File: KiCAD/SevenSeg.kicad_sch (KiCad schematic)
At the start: 34 parts, among them J201 Input, J202 Output, U201 AZ1117-5.0

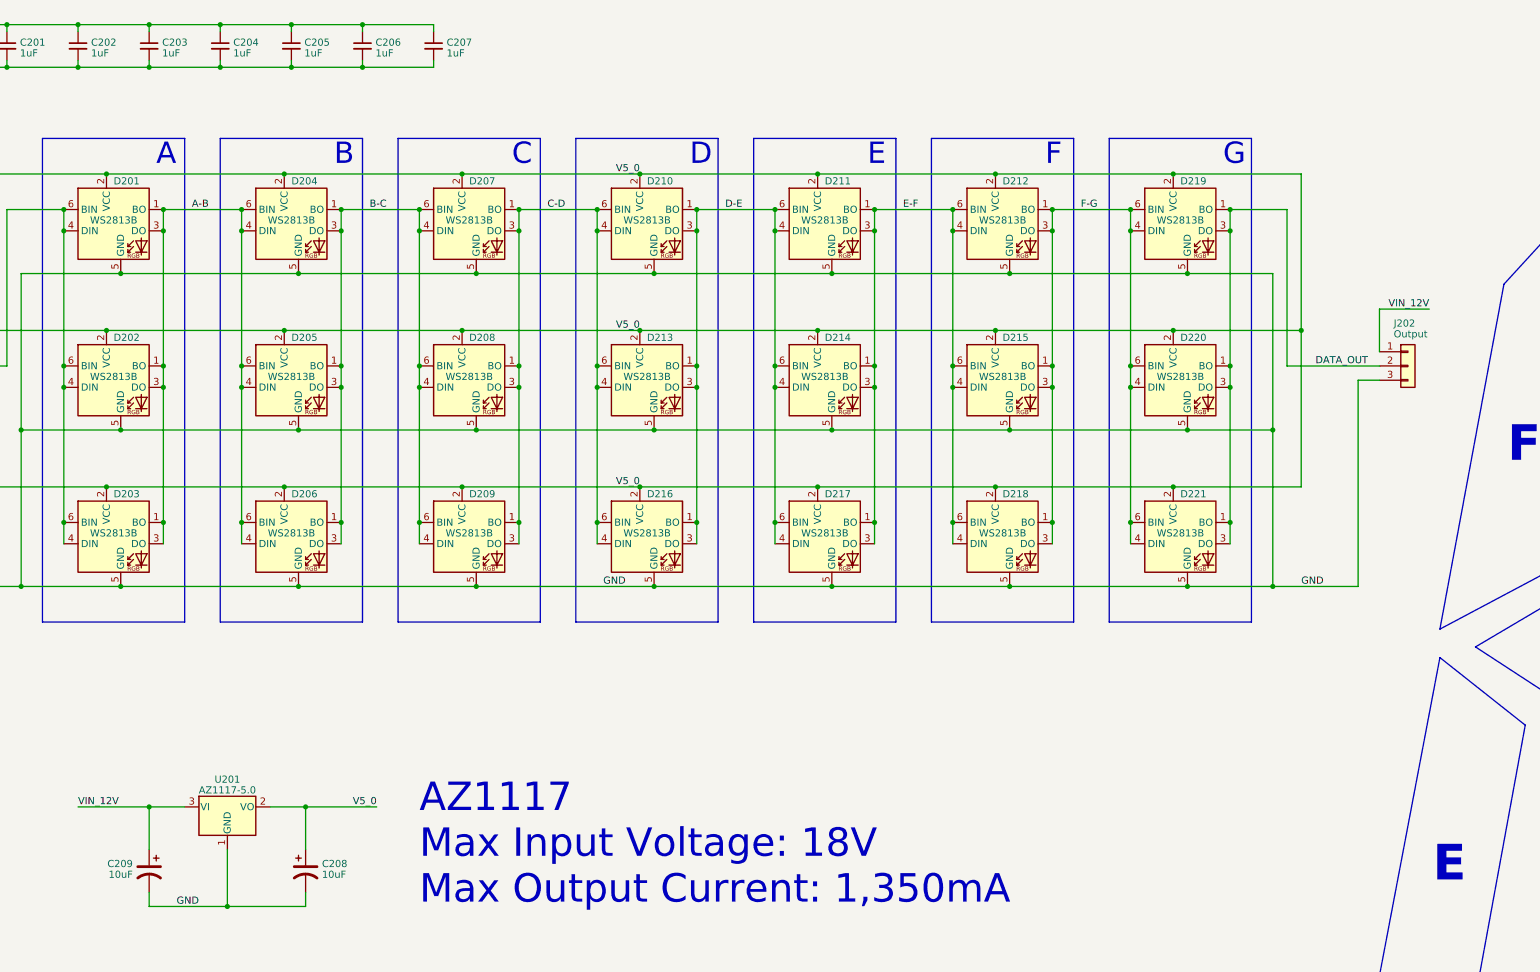
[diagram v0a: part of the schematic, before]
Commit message: Initial PCB layout for 7-seg digits
I realize now that the PCB for the digits needs to be slanted, otherwise the colon pcb won't fit next to it, grumble
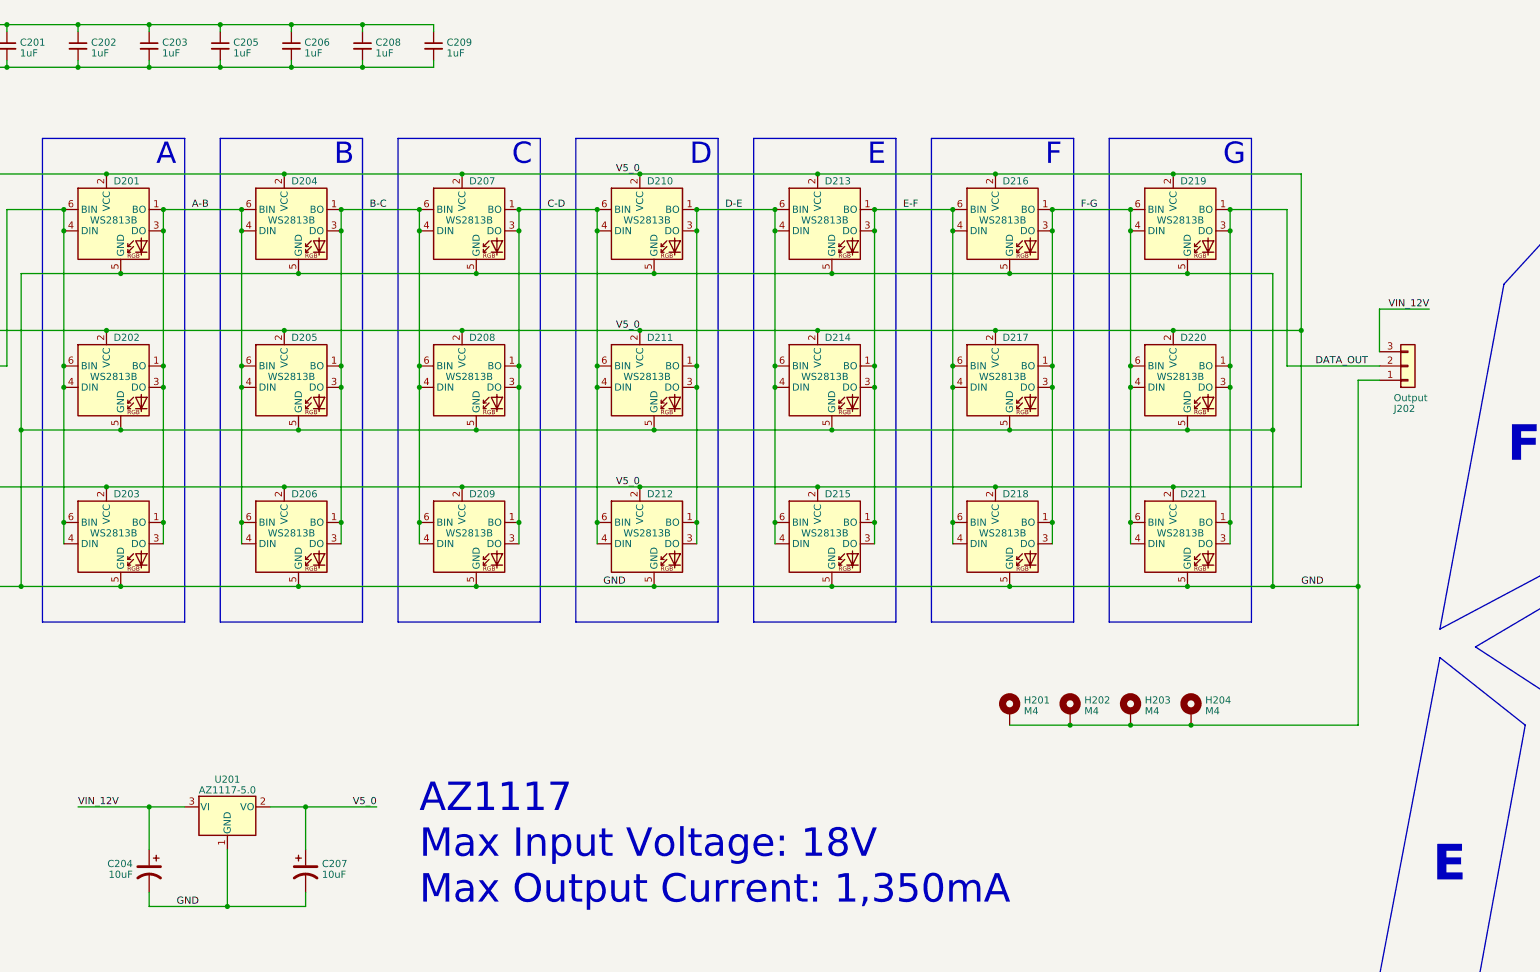
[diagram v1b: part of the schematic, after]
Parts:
- added H201, H202, H203, H204: M4, MountingHole:MountingHole_4.3mm_M4_DIN965_Pad, symbol Mechanical:MountingHole_Pad
- C201, C202, C203: footprint Capacitor_SMD:C_0402_1005Metric_Pad0.74x0.62mm_HandSolder -> Capacitor_SMD:C_0603_1608Metric_Pad1.08x0.95mm_HandSolder
- C205: renamed from C204; footprint Capacitor_SMD:C_0402_1005Metric_Pad0.74x0.62mm_HandSolder -> Capacitor_SMD:C_0603_1608Metric_Pad1.08x0.95mm_HandSolder
- C206: renamed from C205; footprint Capacitor_SMD:C_0402_1005Metric_Pad0.74x0.62mm_HandSolder -> Capacitor_SMD:C_0603_1608Metric_Pad1.08x0.95mm_HandSolder
- C208: renamed from C206; footprint Capacitor_SMD:C_0402_1005Metric_Pad0.74x0.62mm_HandSolder -> Capacitor_SMD:C_0603_1608Metric_Pad1.08x0.95mm_HandSolder
- C209: renamed from C207; footprint Capacitor_SMD:C_0402_1005Metric_Pad0.74x0.62mm_HandSolder -> Capacitor_SMD:C_0603_1608Metric_Pad1.08x0.95mm_HandSolder
- R201: footprint Resistor_SMD:R_0402_1005Metric_Pad0.72x0.64mm_HandSolder -> Resistor_SMD:R_0603_1608Metric_Pad0.98x0.95mm_HandSolder
- renumbered C209 to C204, C208 to C207, D213 to D211, D216 to D212, D211 to D213, D217 to D215, D212 to D216, D215 to D217
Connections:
- net GND: now also J202.1 (Pin_1), H201.1, H202.1, H203.1, H204.1; no longer J202.3 (Pin_3)
- net VIN_12V: now also J202.3 (Pin_3); no longer J202.1 (Pin_1)

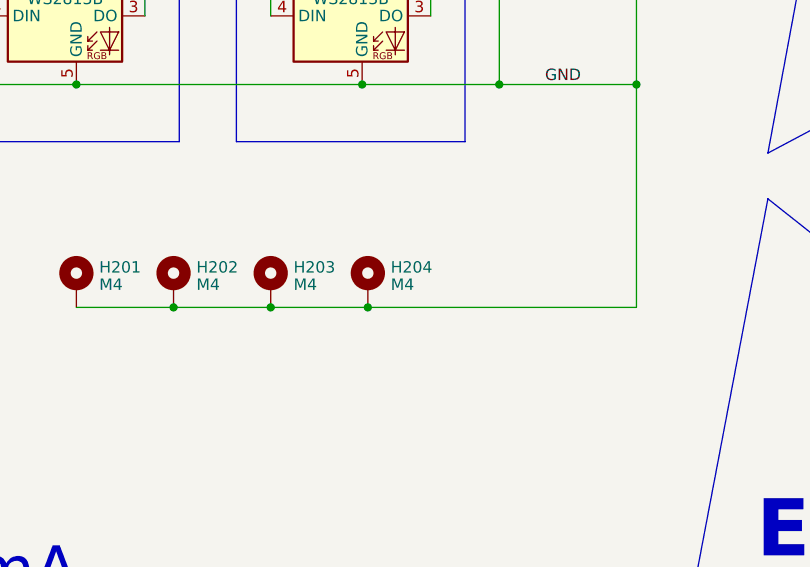
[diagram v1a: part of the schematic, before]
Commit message: Reduced 7-seg mounting holes to 2
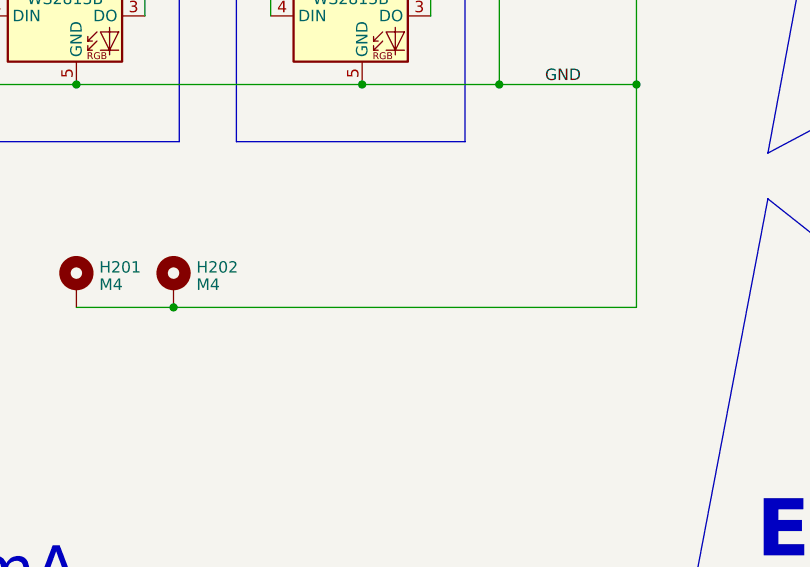
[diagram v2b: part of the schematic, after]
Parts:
- removed H203, H204: M4, MountingHole:MountingHole_4.3mm_M4_DIN965_Pad, symbol Mechanical:MountingHole_Pad
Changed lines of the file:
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@@
   (junction (at 111.76 30.48) (diameter 0) (color 0 0 0 0)
   )
-  (junction (at 259.715 147.955) (diameter 0) (color 0 0 0 1)
-  )
   (junction (at 66.04 105.41) (diameter 0) (color 194 0 0 1)
   )
@@
   (junction (at 185.42 87.63) (diameter 0) (color 0 0 0 0)
   )
-  (junction (at 248.92 147.955) (diameter 0) (color 0 0 0 1)
-  )
   (junction (at 217.17 59.69) (diameter 0) (color 0 0 0 0)
   )
@@
     (stroke (width 0) (type default))
   )
-  (wire (pts (xy 238.125 147.955) (xy 248.92 147.955))
-    (stroke (width 0) (type default) (color 0 0 0 1))
-  )
   (wire (pts (xy 100.33 123.19) (xy 132.08 123.19))
     (stroke (width 0) (type default) (color 0 0 0 1))
@@
     (stroke (width 0) (type default) (color 0 0 0 1))
   )
-  (wire (pts (xy 289.56 147.955) (xy 259.715 147.955))
-    (stroke (width 0) (type default) (color 0 0 0 1))
-  )
   (polyline (pts (xy 402.59 50.8) (xy 408.305 57.15))
     (stroke (width 0) (type default))
@@
     (stroke (width 0) (type default))
   )
-  (wire (pts (xy 248.92 147.955) (xy 259.715 147.955))
+  (wire (pts (xy 238.125 147.955) (xy 289.56 147.955))
     (stroke (width 0) (type default) (color 0 0 0 1))
   )
@@
     (effects (font (size 1.27 1.27)) (justify right bottom))
   )
-  (symbol (lib_id "Mechanical:MountingHole_Pad") (at 248.92 145.415 0) (unit 1)
-    (in_bom yes) (on_board yes) (dnp no) (fields_autoplaced)
-    (property "Reference" "H203" (at 251.46 143.5013 0)
-      (effects (font (size 1.27 1.27)) (justify left))
-    )
-    (property "Value" "M4" (at 251.46 145.4223 0)
-      (effects (font (size 1.27 1.27)) (justify left))
-    )
-    (property "Footprint" "MountingHole:MountingHole_4.3mm_M4_DIN965_Pad" (at 248.92 145.415 0)
-      (effects (font (size 1.27 1.27)) hide)
-    )
-    (property "Datasheet" "~" (at 248.92 145.415 0)
-      (effects (font (size 1.27 1.27)) hide)
-    )
-    (pin "1")
-    (instances
-      (project "SevenSegClock-Main"
-        (path "/2a5cec2f-c9dc-4298-92c3-7c4a8539120b/c210f423-f93a-431e-9b1d-29dff8886738"
-          (reference "H203") (unit 1)
-        )
-      )
-    )
-  )
   (symbol (lib_id "Mechanical:MountingHole_Pad") (at 238.125 145.415 0) (unit 1)
     (in_bom yes) (on_board yes) (dnp no) (fields_autoplaced)
@@
         )
       )
-    )
-  )
-  (symbol (lib_id "Mechanical:MountingHole_Pad") (at 259.715 145.415 0) (unit 1)
-    (in_bom yes) (on_board yes) (dnp no) (fields_autoplaced)
-    (property "Reference" "H204" (at 262.255 143.5013 0)
-      (effects (font (size 1.27 1.27)) (justify left))
-    )
-    (property "Value" "M4" (at 262.255 145.4223 0)
-      (effects (font (size 1.27 1.27)) (justify left))
-    )
-    (property "Footprint" "MountingHole:MountingHole_4.3mm_M4_DIN965_Pad" (at 259.715 145.415 0)
-      (effects (font (size 1.27 1.27)) hide)
-    )
-    (property "Datasheet" "~" (at 259.715 145.415 0)
-      (effects (font (size 1.27 1.27)) hide)
-    )
-    (pin "1")
-    (instances
-      (project "SevenSegClock-Main"
-        (path "/2a5cec2f-c9dc-4298-92c3-7c4a8539120b/c210f423-f93a-431e-9b1d-29dff8886738"
-          (reference "H204") (unit 1)
-        )
-      )
